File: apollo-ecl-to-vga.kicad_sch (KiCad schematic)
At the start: 11 parts, among them IC1 SY100ELT25ZG-TR, J1 DB9_Female, J2 DB15_Female

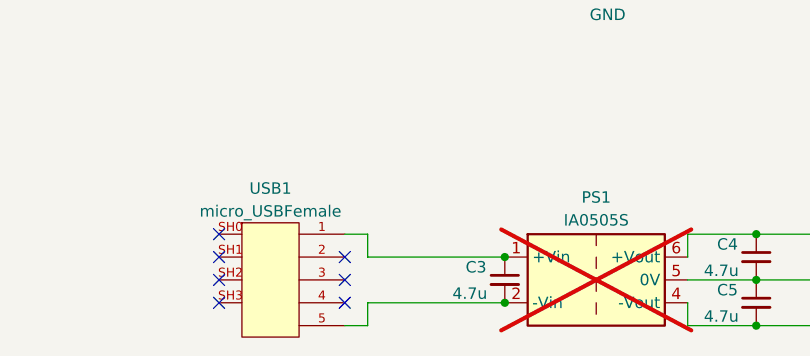
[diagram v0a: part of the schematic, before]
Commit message: label nets from usb connector
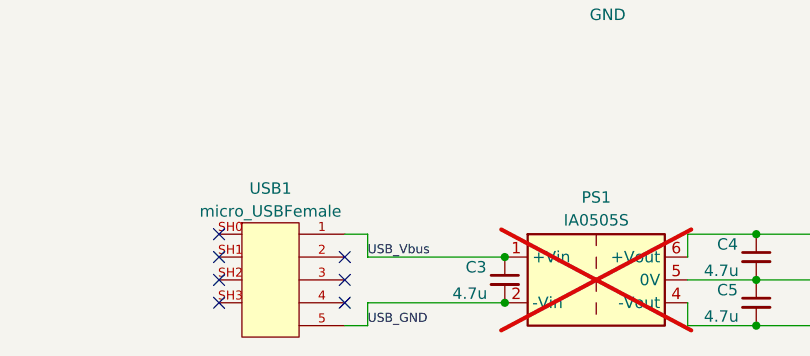
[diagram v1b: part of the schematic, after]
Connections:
- net USB_Vbus: now reaches C3.1, PS1.1 (+Vin), USB1.1 (V+)
- net USB_GND: now reaches C3.2, PS1.2 (-Vin), USB1.5 (V-)
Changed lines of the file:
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@@
     (effects (font (size 1.27 1.27)) (justify left bottom))
+  )
+  (label "USB_GND" (at 120.65 113.03 0) (fields_autoplaced)
+    (effects (font (size 1 1)) (justify left bottom))
   )
   (label "sync_gnd" (at 88.9 57.15 180) (fields_autoplaced)
@@
     (effects (font (size 1 1)) (justify left bottom))
   )
+  (label "USB_Vbus" (at 120.65 105.41 0) (fields_autoplaced)
+    (effects (font (size 1 1)) (justify left bottom))
+  )

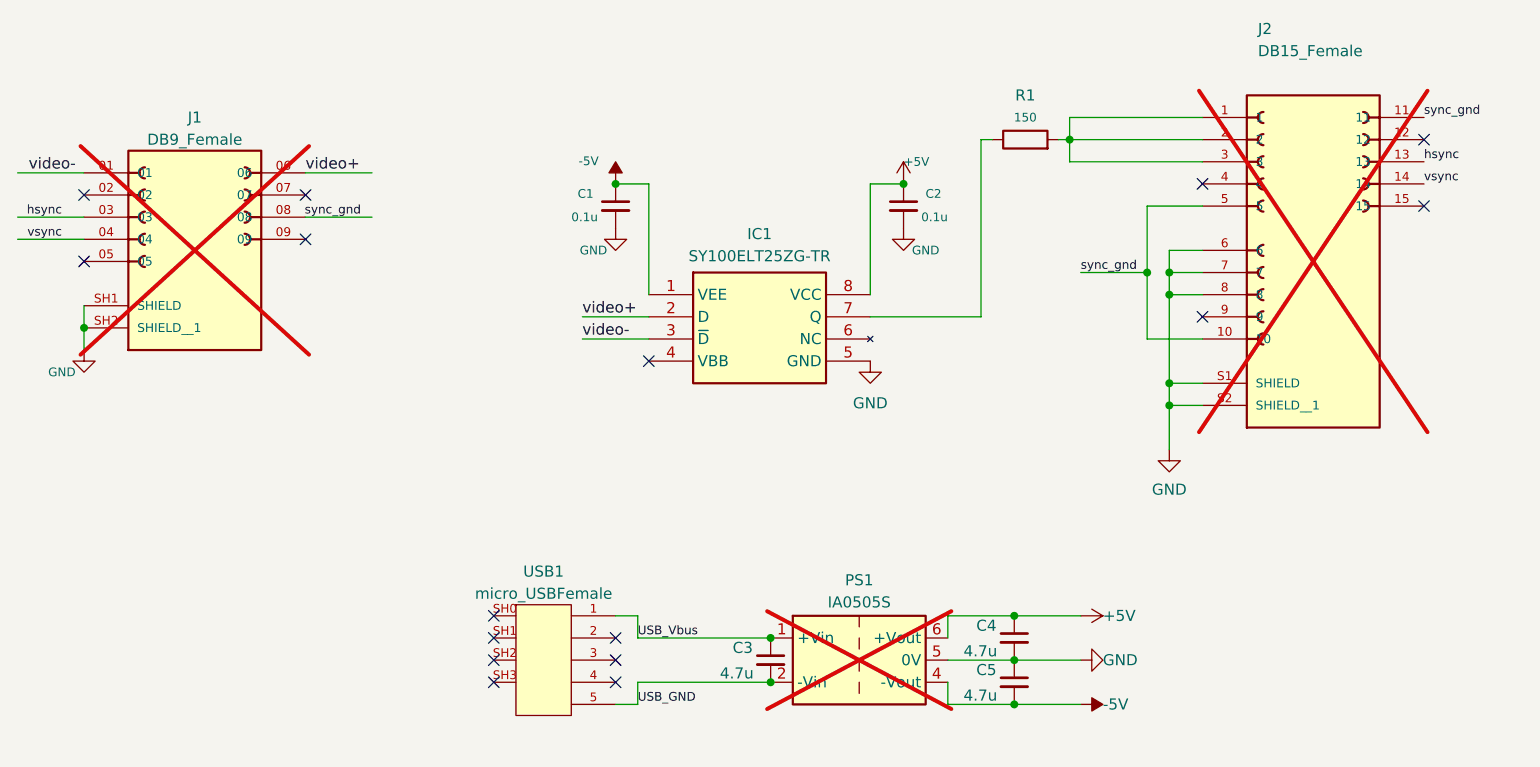
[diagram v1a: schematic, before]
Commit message: add more resistors
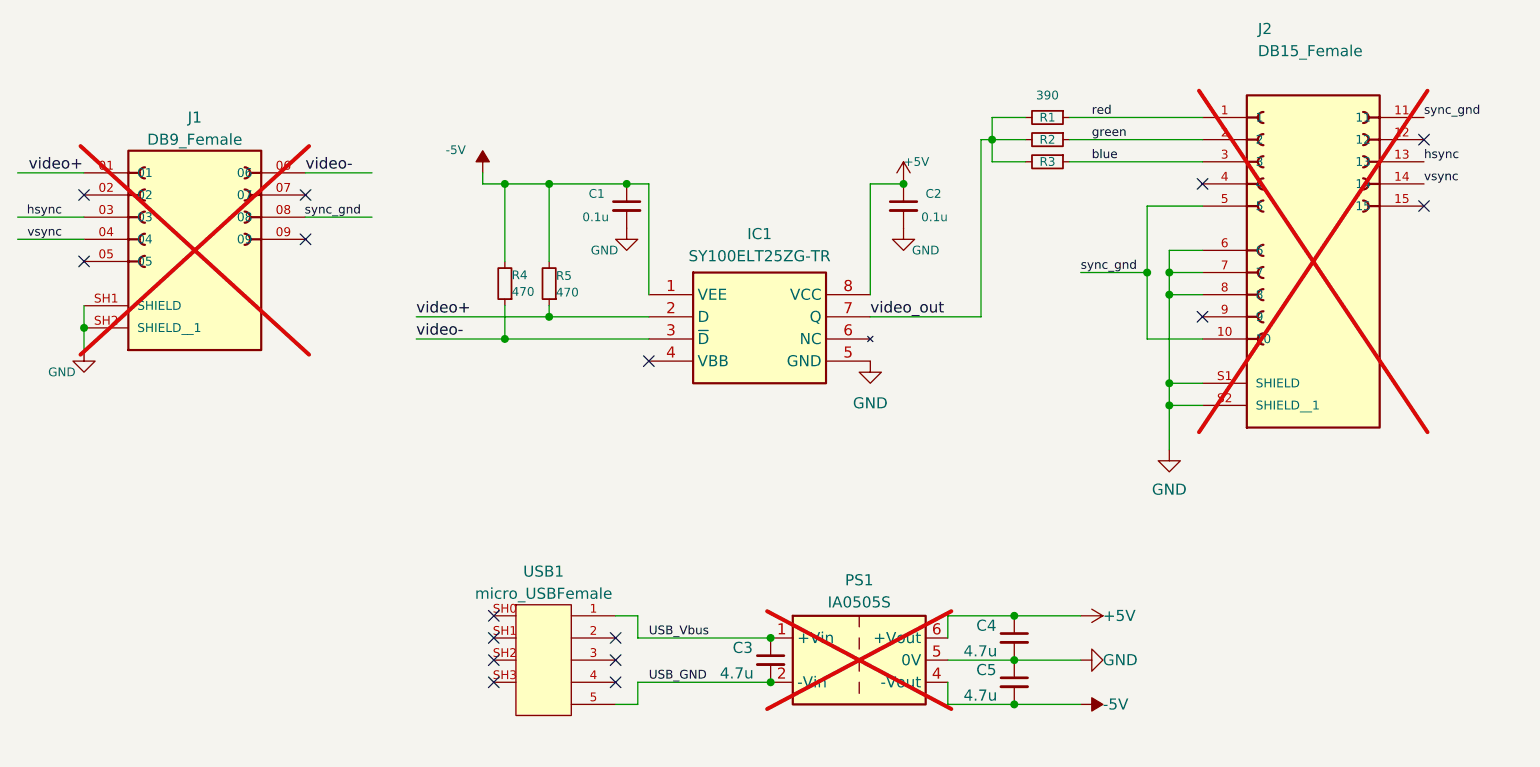
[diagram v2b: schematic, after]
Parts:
- removed R1: 150, Resistor_SMD:R_0805_2012Metric, symbol Device:R
- added R1, R2, R3: 390, Resistor_SMD:R_0603_1608Metric, symbol Device:R_Small
- added R4, R5: 470, Resistor_SMD:R_0603_1608Metric, symbol Device:R_Small
- C1: footprint Capacitor_SMD:C_0603_1608Metric -> Resistor_SMD:R_0603_1608Metric
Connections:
- net -5V: now also R4.2, R5.2
- net video+: now also J1.01, R5.1; no longer J1.06
- net video-: now also J1.06, R4.1; no longer J1.01
- net video_out: now reaches IC1.7 (Q)
- net video_out: now also R1.2, R2.2, R3.2
- new net blue: J2.3, R3.1
- new net green: J2.2, R2.1
- new net red: J2.1, R1.1

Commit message: single GND.  move things (vias, resistors, DC/DC) a touch to clean up routing, and cleanup some trace widths
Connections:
- net USB_GND is gone; now on net GND: C3.2, PS1.2 (-Vin), USB1.5 (V-)
- net sync_gnd is gone; now on net GND: J1.08, J2.10, J2.11, J2.5
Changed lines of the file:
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@@
   (junction (at 105.41 53.34) (diameter 0) (color 0 0 0 0)
   )
-  (junction (at 179.07 63.5) (diameter 0) (color 0 0 0 0)
+  (junction (at 163.83 102.87) (diameter 0) (color 0 0 0 0)
   )
   (junction (at 135.89 110.49) (diameter 0) (color 0 0 0 0)
   )
-  (junction (at 163.83 102.87) (diameter 0) (color 0 0 0 0)
-  )
   (junction (at 181.61 66.04) (diameter 0) (color 0 0 0 0)
   )
@@
   (junction (at 151.13 53.34) (diameter 0) (color 0 0 0 0)
   )
+  (junction (at 181.61 71.12) (diameter 0) (color 0 0 0 0)
+  )
   (junction (at 163.83 113.03) (diameter 0) (color 0 0 0 0)
+  )
+  (junction (at 181.61 60.96) (diameter 0) (color 0 0 0 0)
   )
   (no_connect (at 185.42 68.58))
@@
   (no_connect (at 210.82 55.88))
   (no_connect (at 185.42 53.34))
-  (wire (pts (xy 181.61 66.04) (xy 181.61 76.2))
+  (wire (pts (xy 181.61 66.04) (xy 181.61 71.12))
     (stroke (width 0) (type default))
   )
@@
     (stroke (width 0) (type default))
   )
+  (wire (pts (xy 185.42 55.88) (xy 181.61 55.88))
+    (stroke (width 0) (type default))
+  )
   (wire (pts (xy 110.49 53.34) (xy 110.49 62.23))
     (stroke (width 0) (type default))
@@
     (stroke (width 0) (type default))
   )
+  (wire (pts (xy 210.82 45.72) (xy 219.71 45.72))
+    (stroke (width 0) (type default))
+  )
   (wire (pts (xy 181.61 60.96) (xy 181.61 63.5))
     (stroke (width 0) (type default))
@@
     (stroke (width 0) (type default))
   )
+  (wire (pts (xy 181.61 71.12) (xy 185.42 71.12))
+    (stroke (width 0) (type default))
+  )
   (wire (pts (xy 161.29 50.8) (xy 165.1 50.8))
     (stroke (width 0) (type default))
@@
     (stroke (width 0) (type default))
   )
-  (wire (pts (xy 179.07 55.88) (xy 179.07 63.5))
-    (stroke (width 0) (type default))
-  )
   (wire (pts (xy 170.18 50.8) (xy 185.42 50.8))
     (stroke (width 0) (type default))
   )
-  (wire (pts (xy 179.07 63.5) (xy 179.07 71.12))
-    (stroke (width 0) (type default))
-  )
   (wire (pts (xy 95.25 71.12) (xy 105.41 71.12))
     (stroke (width 0) (type default))
@@
     (stroke (width 0) (type default))
   )
-  (wire (pts (xy 120.65 110.49) (xy 135.89 110.49))
-    (stroke (width 0) (type default))
-  )
   (wire (pts (xy 181.61 78.74) (xy 181.61 83.82))
     (stroke (width 0) (type default))
@@
     (stroke (width 0) (type default))
   )
+  (wire (pts (xy 181.61 71.12) (xy 181.61 76.2))
+    (stroke (width 0) (type default))
+  )
   (wire (pts (xy 160.02 48.26) (xy 160.02 68.58))
     (stroke (width 0) (type default))
@@
     (stroke (width 0) (type default))
   )
-  (wire (pts (xy 179.07 55.88) (xy 185.42 55.88))
-    (stroke (width 0) (type default))
-  )
   (wire (pts (xy 170.18 48.26) (xy 185.42 48.26))
     (stroke (width 0) (type default))
   )
-  (wire (pts (xy 118.11 113.03) (xy 120.65 113.03))
-    (stroke (width 0) (type default))
-  )
   (wire (pts (xy 120.65 105.41) (xy 135.89 105.41))
     (stroke (width 0) (type default))
@@
     (stroke (width 0) (type default))
   )
+  (wire (pts (xy 82.55 57.15) (xy 86.995 57.15))
+    (stroke (width 0) (type default))
+  )
   (wire (pts (xy 161.29 48.26) (xy 161.29 50.8))
     (stroke (width 0) (type default))
@@
     (stroke (width 0) (type default))
   )
-  (wire (pts (xy 120.65 110.49) (xy 120.65 113.03))
-    (stroke (width 0) (type default))
-  )
-  (wire (pts (xy 90.17 57.15) (xy 82.55 57.15))
-    (stroke (width 0) (type default))
-  )
   (wire (pts (xy 147.32 66.04) (xy 147.32 53.34))
     (stroke (width 0) (type default))
@@
     (stroke (width 0) (type default))
   )
+  (wire (pts (xy 181.61 55.88) (xy 181.61 60.96))
+    (stroke (width 0) (type default))
+  )
   (wire (pts (xy 49.53 59.69) (xy 57.15 59.69))
     (stroke (width 0) (type default))
@@
     (stroke (width 0) (type default))
   )
-  (wire (pts (xy 179.07 71.12) (xy 185.42 71.12))
-    (stroke (width 0) (type default))
-  )
   (wire (pts (xy 102.87 53.34) (xy 105.41 53.34))
     (stroke (width 0) (type default))
@@
   )
   (wire (pts (xy 161.29 48.26) (xy 165.1 48.26))
-    (stroke (width 0) (type default))
-  )
-  (wire (pts (xy 171.45 63.5) (xy 179.07 63.5))
     (stroke (width 0) (type default))
   )
@@
     (effects (font (size 1.27 1.27)) (justify left bottom))
   )
-  (label "USB_GND" (at 121.92 110.49 0) (fields_autoplaced)
-    (effects (font (size 1 1)) (justify left bottom))
-  )
-  (label "sync_gnd" (at 88.9 57.15 180) (fields_autoplaced)
-    (effects (font (size 1 1)) (justify right bottom))
-  )
   (label "vsync" (at 54.61 59.69 180) (fields_autoplaced)
     (effects (font (size 1 1)) (justify right bottom))
@@
     (effects (font (size 1 1)) (justify left bottom))
   )
-  (label "sync_gnd" (at 210.82 45.72 0) (fields_autoplaced)
-    (effects (font (size 1 1)) (justify left bottom))
-  )
   (label "red" (at 172.72 45.72 0) (fields_autoplaced)
     (effects (font (size 1 1)) (justify left bottom))
@@
   )
   (label "USB_Vbus" (at 121.92 105.41 0) (fields_autoplaced)
-    (effects (font (size 1 1)) (justify left bottom))
-  )
-  (label "sync_gnd" (at 171.45 63.5 0) (fields_autoplaced)
     (effects (font (size 1 1)) (justify left bottom))
   )
@@
     )
   )
+  (symbol (lib_id "power:GND") (at 118.11 113.03 0) (unit 1)
+    (in_bom yes) (on_board yes) (dnp no)
+    (property "Reference" "#PWR010" (at 118.11 119.38 0)
+      (effects (font (size 1.27 1.27)) hide)
+    )
+    (property "Value" "GND" (at 120.65 116.84 0)
+      (effects (font (size 1.27 1.27)) (justify right))
+    )
+    (property "Footprint" "" (at 118.11 113.03 0)
+      (effects (font (size 1.27 1.27)) hide)
+    )
+    (property "Datasheet" "" (at 118.11 113.03 0)
+      (effects (font (size 1.27 1.27)) hide)
+    )
+    (pin "1")
+    (instances
+      (project "apollo-ecl-to-vga"
+        (path "/c8c8cd56-af04-4a7d-b456-961da97c5033"
+          (reference "#PWR010") (unit 1)
+        )
+      )
+    )
+  )
   (symbol (lib_id "Device:C_Small") (at 163.83 105.41 0) (unit 1)
     (in_bom yes) (on_board yes) (dnp no)
@@
         (path "/c8c8cd56-af04-4a7d-b456-961da97c5033"
           (reference "#PWR08") (unit 1)
+        )
+      )
+    )
+  )
+  (symbol (lib_id "power:GND") (at 135.89 110.49 0) (unit 1)
+    (in_bom yes) (on_board yes) (dnp no)
+    (property "Reference" "#PWR012" (at 135.89 116.84 0)
+      (effects (font (size 1.27 1.27)) hide)
+    )
+    (property "Value" "GND" (at 138.43 114.3 0)
+      (effects (font (size 1.27 1.27)) (justify right))
+    )
+    (property "Footprint" "" (at 135.89 110.49 0)
+      (effects (font (size 1.27 1.27)) hide)
+    )
+    (property "Datasheet" "" (at 135.89 110.49 0)
+      (effects (font (size 1.27 1.27)) hide)
+    )
+    (pin "1")
+    (instances
+      (project "apollo-ecl-to-vga"
+        (path "/c8c8cd56-af04-4a7d-b456-961da97c5033"
+          (reference "#PWR012") (unit 1)
         )
       )
@@
     )
   )
+  (symbol (lib_id "power:GND") (at 86.995 57.15 0) (unit 1)
+    (in_bom yes) (on_board yes) (dnp no) (fields_autoplaced)
+    (property "Reference" "#PWR014" (at 86.995 63.5 0)
+      (effects (font (size 1.27 1.27)) hide)
+    )
+    (property "Value" "GND" (at 86.995 61.722 0)
+      (effects (font (size 1.27 1.27)))
+    )
+    (property "Footprint" "" (at 86.995 57.15 0)
+      (effects (font (size 1.27 1.27)) hide)
+    )
+    (property "Datasheet" "" (at 86.995 57.15 0)
+      (effects (font (size 1.27 1.27)) hide)
+    )
+    (pin "1")
+    (instances
+      (project "apollo-ecl-to-vga"
+        (path "/c8c8cd56-af04-4a7d-b456-961da97c5033"
+          (reference "#PWR014") (unit 1)
+        )
+      )
+    )
+  )
   (symbol (lib_id "power:GND") (at 171.45 107.95 90) (unit 1)
     (in_bom yes) (on_board yes) (dnp no)
@@
         )
       )
+    )
+  )
+  (symbol (lib_id "power:GND") (at 219.71 45.72 0) (unit 1)
+    (in_bom yes) (on_board yes) (dnp no) (fields_autoplaced)
+    (property "Reference" "#PWR013" (at 219.71 52.07 0)
+      (effects (font (size 1.27 1.27)) hide)
+    )
+    (property "Value" "GND" (at 219.71 50.8 0)
+      (effects (font (size 1.27 1.27)))
+    )
+    (property "Footprint" "" (at 219.71 45.72 0)
+      (effects (font (size 1.27 1.27)) hide)
+    )
+    (property "Datasheet" "" (at 219.71 45.72 0)
+      (effects (font (size 1.27 1.27)) hide)
+    )
+    (pin "1")
+    (instances
+      (project "apollo-ecl-to-vga"
+        (path "/c8c8cd56-af04-4a7d-b456-961da97c5033"
+          (reference "#PWR013") (unit 1)
+        )
+      )

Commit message: switch from 0805 to 0603 since they're being assembled anyway
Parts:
- C3, C4, C5: footprint Capacitor_SMD:C_0805_2012Metric -> Capacitor_SMD:C_0603_1608Metric
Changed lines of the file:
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@@
       (effects (font (size 1.27 1.27)) (justify left))
     )
-    (property "Footprint" "Capacitor_SMD:C_0805_2012Metric" (at 163.83 110.49 0)
+    (property "Footprint" "Capacitor_SMD:C_0603_1608Metric" (at 163.83 110.49 0)
       (effects (font (size 1.27 1.27)) hide)
     )
@@
       (effects (font (size 1.27 1.27)) (justify left))
     )
-    (property "Footprint" "Capacitor_SMD:C_0805_2012Metric" (at 163.83 105.41 0)
+    (property "Footprint" "Capacitor_SMD:C_0603_1608Metric" (at 163.83 105.41 0)
       (effects (font (size 1.27 1.27)) hide)
     )
@@
       (effects (font (size 1.27 1.27)) (justify left))
     )
-    (property "Footprint" "Capacitor_SMD:C_0805_2012Metric" (at 135.89 107.95 0)
-      (effects (font (size 1.27 1.27)) hide)
-    )
+    (property "Footprint" "Capacitor_SMD:C_0603_1608Metric" (at 135.89 107.95 0)
+      (effects (font (size 1.27 1.27)) hide)
+    )
